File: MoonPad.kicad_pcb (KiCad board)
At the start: 4 copper layers, 44.4 x 40.6 mm, 61 parts, among them IC1 W25Q16JVUXIQ, J1 OLED, J3 USB-C 2.0 Receptacle, SW1 Reset, U3 RP2040, U4 Hall_Sensor, U5 Hall_Sensor, U6 AP2112K-3.3, Y1 JGHC S3212000181080

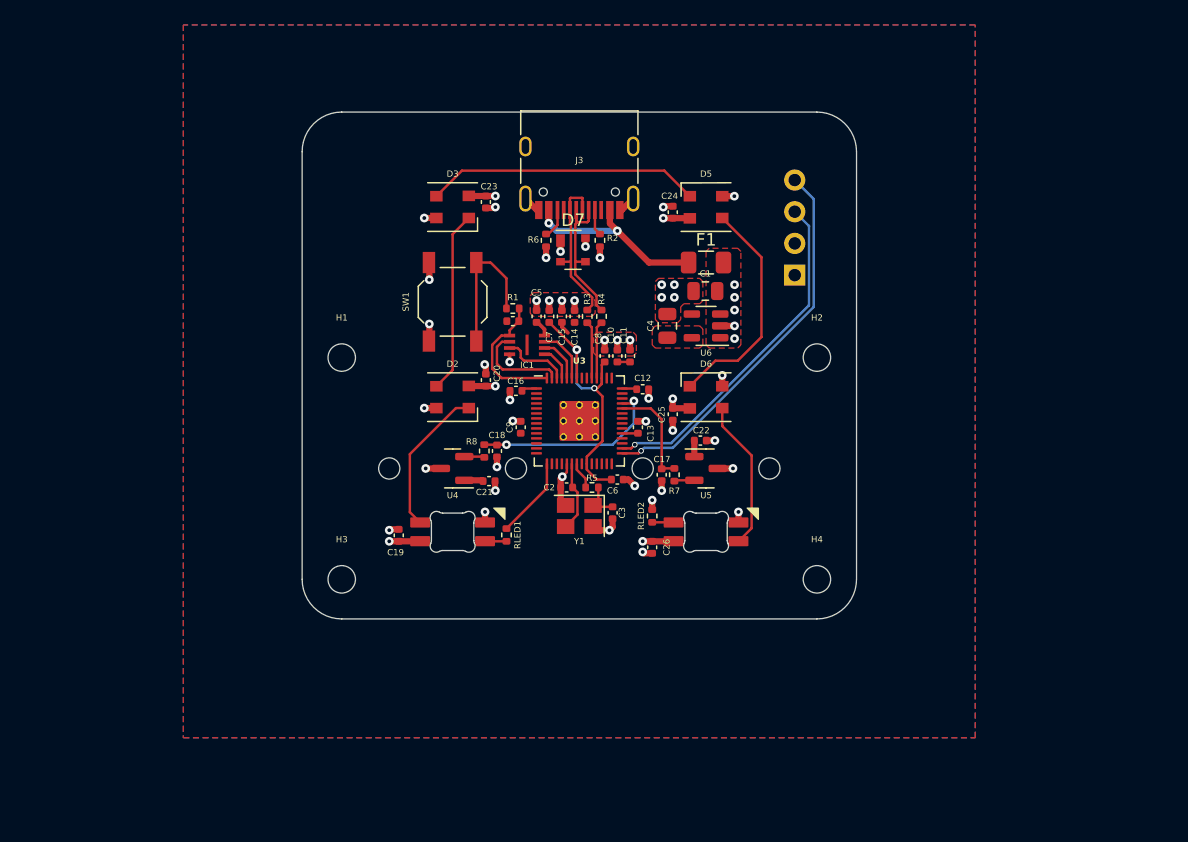
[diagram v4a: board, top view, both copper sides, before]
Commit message: Added part numbers, some schema adjustments
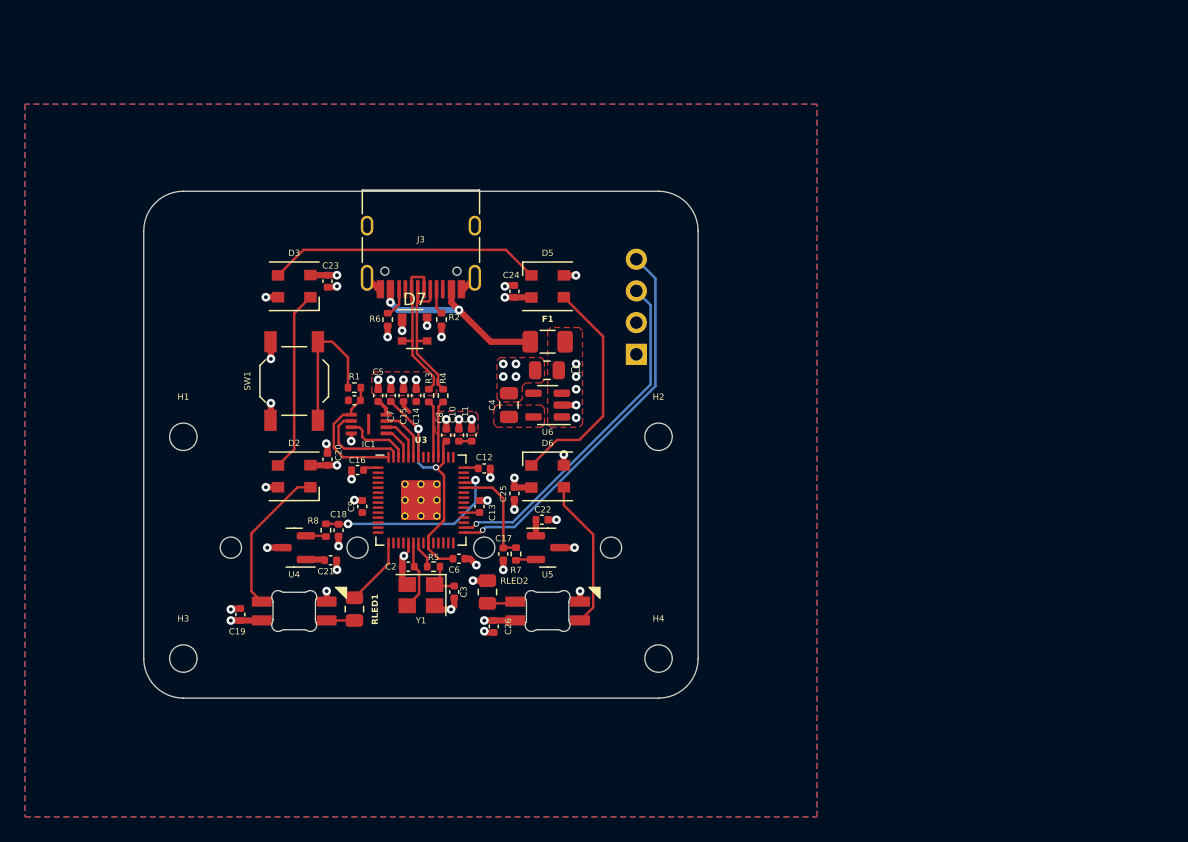
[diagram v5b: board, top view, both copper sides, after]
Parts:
- RLED1, RLED2: footprint Resistor_SMD:R_0402_1005Metric -> Resistor_SMD:R_0805_2012Metric
- moved RLED2 14.5 mm to (151.4, 109.0)
- moved C12 14.2 mm to (151.1, 99.1)
- moved C13 14.2 mm to (150.7, 102.1)
- moved C15 14.2 mm to (144.7, 93.2)
- moved C17 14.2 mm to (152.7, 105.9)
- moved C23 14.2 mm to (138.6, 84.0)
- moved C1 14.2 mm to (156.2, 91.2)
- moved C2 14.2 mm to (145.0, 106.9)
- moved C20 14.2 mm to (138.6, 98.3)
- moved C26 14.2 mm to (151.9, 111.7)
- moved C8 14.2 mm to (148.1, 96.4)
- moved D1 14.2 mm to (135.9, 105.4)
- moved D2 14.2 mm to (135.9, 99.7)
- moved D3 14.2 mm to (135.9, 84.5)
- moved H2 14.2 mm to (165.1, 96.5)
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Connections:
- net /GPIO12 renamed /RGB
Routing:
- net /RGB: track 6.54 -> 5.52 mm
- net Net-(D4-DOUT): track 1.72 -> 2.28 mm
- net Net-(D1-DIN): track 1.72 -> 2.23 mm
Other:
- board size 44.4 x 40.6 mm -> 44.5 x 40.6 mm

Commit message: Minor layout changes
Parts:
- moved C26 0.68 mm to (151.4, 111.3), turned to 180 degrees
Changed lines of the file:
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@@
     (property "ki_keywords" "cap capacitor")
     (attr smd)
-    (fp_text reference "C9" (at 0 -0.889 90) (layer "F.SilkS")
+    (fp_text reference "C9" (at 1.27 0 180) (layer "F.SilkS")
         (effects (font (size 0.5 0.5) (thickness 0.125)))
     )
@@
   )
   (footprint "Capacitor_SMD:C_0402_1005Metric" (layer "F.Cu")
-    (at 151.892 111.732 -90)
+    (at 151.412 111.252 180)
     (descr "Capacitor SMD 0402 (1005 Metric), square (rectangular) end terminal, IPC_7351 nominal, (Body size source: IPC-SM-782 page 76, https://www.pcb-3d.com/wordpress/wp-content/uploads/ipc-sm-782a_amendment_1_and_2.pdf), generated with kicad-footprint-generator")
     (tags "capacitor")
@@
     (property "ki_keywords" "cap capacitor")
     (attr smd)
-    (fp_text reference "C26" (at 0 -1.16 90) (layer "F.SilkS")
+    (fp_text reference "C26" (at 1.679 0) (layer "F.SilkS")
         (effects (font (size 0.5 0.5) (thickness 0.125)))
     )
-    (fp_text value "100n" (at 0 1.16 90) (layer "F.Fab")
+    (fp_text value "100n" (at 0 1.16) (layer "F.Fab")
         (effects (font (size 1 1) (thickness 0.15)))
     )
-    (fp_text user "${REFERENCE}" (at 0 0 90) (layer "F.Fab")
+    (fp_text user "${REFERENCE}" (at 0 0) (layer "F.Fab")
         (effects (font (size 0.25 0.25) (thickness 0.04)))
     )
@@
     (fp_line (start 0.5 0.25) (end -0.5 0.25)
       (stroke (width 0.1) (type solid)) (layer "F.Fab"))
-    (pad "1" smd roundrect (at -0.48 0 270) (size 0.56 0.62) (layers "F.Cu" "F.Paste" "F.Mask") (roundrect_rratio 0.25)
+    (pad "1" smd roundrect (at -0.48 0 180) (size 0.56 0.62) (layers "F.Cu" "F.Paste" "F.Mask") (roundrect_rratio 0.25)
       (net 1 "VBUS") (pintype "passive"))
-    (pad "2" smd roundrect (at 0.48 0 270) (size 0.56 0.62) (layers "F.Cu" "F.Paste" "F.Mask") (roundrect_rratio 0.25)
+    (pad "2" smd roundrect (at 0.48 0 180) (size 0.56 0.62) (layers "F.Cu" "F.Paste" "F.Mask") (roundrect_rratio 0.25)
       (net 2 "GND") (pintype "passive"))
     (model "${KICAD6_3DMODEL_DIR}/Capacitor_SMD.3dshapes/C_0402_1005Metric.wrl"
@@
     (property "ki_keywords" "cap capacitor")
     (attr smd)
-    (fp_text reference "C20" (at 0.536 0.889 270) (layer "F.SilkS")
+    (fp_text reference "C20" (at 0.536 0.889 90) (layer "F.SilkS")
         (effects (font (size 0.5 0.5) (thickness 0.125)))
     )
@@
     (property "ki_keywords" "cap capacitor")
     (attr smd)
-    (fp_text reference "C3" (at 0 -0.762 90) (layer "F.SilkS")
+    (fp_text reference "C3" (at 0 -1.016 -180) (layer "F.SilkS")
         (effects (font (size 0.5 0.5) (thickness 0.125)))
     )
@@
     (property "Sheetname" "")
     (attr smd)
-    (fp_text reference "U3" (at 0 -4.82) (layer "F.SilkS")
+    (fp_text reference "U3" (at 0 -4.572) (layer "F.SilkS")
         (effects (font (size 0.5 0.5) (thickness 0.125) bold))
     )
@@
     (property "ki_keywords" "R res resistor")
     (attr smd)
-    (fp_text reference "R5" (at 0 -0.762) (layer "F.SilkS")
+    (fp_text reference "R5" (at 0 -0.889) (layer "F.SilkS")
         (effects (font (size 0.5 0.5) (thickness 0.125)))
     )
@@
     (fp_arc (start -1.699999 -4.377158) (mid -1.712527 -4.265932) (end -1.749484 -4.16028)
       (stroke (width 0.1) (type solid)) (layer "Edge.Cuts"))
-    (fp_arc (start -1.046711 -3.511701) (mid -1.638072 -3.575966) (end -1.749484 -4.160281)
+    (fp_arc (start -1.046711 -3.511701) (mid -1.638071 -3.575966) (end -1.749484 -4.160281)
       (stroke (width 0.1) (type solid)) (layer "Edge.Cuts"))
     (fp_arc (start -1.046711 -3.511701) (mid -0.925123 -3.562624) (end -0.794452 -3.58)
@@
     (fp_arc (start 1.046711 -6.648299) (mid 1.638071 -6.584036) (end 1.749484 -5.99972)
       (stroke (width 0.1) (type solid)) (layer "Edge.Cuts"))
-    (fp_arc (start 1.699999 -5.782842) (mid 1.712528 -5.894068) (end 1.749484 -5.99972)
+    (fp_arc (start 1.699999 -5.782842) (mid 1.712527 -5.894068) (end 1.749484 -5.99972)
       (stroke (width 0.1) (type solid)) (layer "Edge.Cuts"))
     (fp_arc (start 1.749484 -4.16028) (mid 1.63807 -3.575966) (end 1.046711 -3.511703)
@@
     (fp_arc (start -1.699999 -4.377158) (mid -1.712527 -4.265932) (end -1.749484 -4.16028)
       (stroke (width 0.1) (type solid)) (layer "Edge.Cuts"))
-    (fp_arc (start -1.046711 -3.511701) (mid -1.638072 -3.575966) (end -1.749484 -4.160281)
+    (fp_arc (start -1.046711 -3.511701) (mid -1.638071 -3.575966) (end -1.749484 -4.160281)
       (stroke (width 0.1) (type solid)) (layer "Edge.Cuts"))
     (fp_arc (start -1.046711 -3.511701) (mid -0.925123 -3.562624) (end -0.794452 -3.58)
@@
     (fp_arc (start 1.046711 -6.648299) (mid 1.638071 -6.584036) (end 1.749484 -5.99972)
       (stroke (width 0.1) (type solid)) (layer "Edge.Cuts"))
-    (fp_arc (start 1.699999 -5.782842) (mid 1.712528 -5.894068) (end 1.749484 -5.99972)
+    (fp_arc (start 1.699999 -5.782842) (mid 1.712527 -5.894068) (end 1.749484 -5.99972)
       (stroke (width 0.1) (type solid)) (layer "Edge.Cuts"))
     (fp_arc (start 1.749484 -4.16028) (mid 1.63807 -3.575966) (end 1.046711 -3.511703)
@@
       (rotate (xyz 0 0 0))
     )
+    (model "${KIPRJMOD}/Libraries/kicad-keyboard-parts.pretty/3d/LED_SK6812MINI-E.step"
+      (offset (xyz 0 0 0))
+      (scale (xyz 1 1 1))
+      (rotate (xyz 0 0 0))
+    )
   )
   (footprint "Button_Switch_Keyboard:Wooting_1.00u" (layer "B.Cu")
@@
   (segment (start 131.572 111.252) (end 133.278 111.252) (width 0.5) (layer "F.Cu") (net 1))
   (segment (start 153.543 100.584) (end 154.899 100.584) (width 0.5) (layer "F.Cu") (net 1))
-  (segment (start 151.892 111.252) (end 151.13 111.252) (width 0.5) (layer "F.Cu") (net 1))
+  (segment (start 151.892 111.252) (end 151.892 112.014) (width 0.5) (layer "F.Cu") (net 1))
   (segment (start 138.557 98.806) (end 139.319 98.806) (width 0.5) (layer "F.Cu") (net 1))
   (segment (start 138.557 83.566) (end 137.201 83.566) (width 0.5) (layer "F.Cu") (net 1))
@@
   (via (at 139.319 83.566) (size 0.7) (drill 0.3) (layers "F.Cu" "B.Cu") (net 1))
   (via (at 158.496 91.694) (size 0.7) (drill 0.3) (layers "F.Cu" "B.Cu") (free) (net 1))
-  (via (at 151.13 111.252) (size 0.7) (drill 0.3) (layers "F.Cu" "B.Cu") (net 1))
+  (via (at 151.892 112.014) (size 0.7) (drill 0.3) (layers "F.Cu" "B.Cu") (net 1))
   (via (at 146.542 87.614) (size 0.7) (drill 0.3) (layers "F.Cu" "B.Cu") (net 1))
   (via (at 158.496 94.995996) (size 0.7) (drill 0.3) (layers "F.Cu" "B.Cu") (free) (net 1))
@@
   (via (at 130.81 111.252) (size 0.7) (drill 0.3) (layers "F.Cu" "B.Cu") (net 1))
   (via (at 158.496001 90.678) (size 0.7) (drill 0.3) (layers "F.Cu" "B.Cu") (free) (net 1))
+  (segment (start 150.932 111.905903) (end 150.932 111.252) (width 0.5) (layer "F.Cu") (net 2))
   (segment (start 144.554 107.974) (end 144.554 106.934) (width 0.5) (layer "F.Cu") (net 2))
   (segment (start 139.446 104.493) (end 139.446 105.283) (width 0.5) (layer "F.Cu") (net 2))
@@
   (segment (start 139.291 107.16) (end 139.319 107.188) (width 0.5) (layer "F.Cu") (net 2))
   (segment (start 152.852 84.384) (end 152.781 84.455) (width 0.5) (layer "F.Cu") (net 2))
+  (segment (start 151.040097 112.014) (end 150.932 111.905903) (width 0.5) (layer "F.Cu") (net 2))
   (segment (start 148.082 95.913) (end 148.082 95.123) (width 0.5) (layer "F.Cu") (net 2))
   (segment (start 133.618 85.33) (end 134.59 85.33) (width 0.5) (layer "F.Cu") (net 2))
@@
   (segment (start 150.2175 108.0535) (end 151.384 108.0535) (width 0.5) (layer "F.Cu") (net 2))
   (segment (start 144.687289 106.070887) (end 144.554 106.204176) (width 0.5) (layer "F.Cu") (net 2))
-  (segment (start 151.238097 112.212) (end 151.892 112.212) (width 0.5) (layer "F.Cu") (net 2))
   (segment (start 151.61 99.794) (end 151.61 99.06) (width 0.5) (layer "F.Cu") (net 2))
   (segment (start 149.455 84.69) (end 150.37 83.775) (width 0.5) (layer "F.Cu") (net 2))
@@
   (segment (start 134.026102 88.900001) (end 134.026103 90.267) (width 0.5) (layer "F.Cu") (net 2))
   (segment (start 158.81 108.894135) (end 158.81 109.74) (width 0.5) (layer "F.Cu") (net 2))
-  (segment (start 151.13 112.103903) (end 151.238097 112.212) (width 0.5) (layer "F.Cu") (net 2))
   (segment (start 149.987 106.299) (end 150.495 106.807) (width 0.5) (layer "F.Cu") (net 2))
   (segment (start 147.443 110.363) (end 147.15 110.07) (width 0.5) (layer "F.Cu") (net 2))
@@
   (via (at 148.082 95.123) (size 0.7) (drill 0.3) (layers "F.Cu" "B.Cu") (net 2))
   (via (at 152.781 84.455) (size 0.7) (drill 0.3) (layers "F.Cu" "B.Cu") (net 2))
-  (via (at 151.13 112.103903) (size 0.7) (drill 0.3) (layers "F.Cu" "B.Cu") (net 2))
+  (via (at 151.040097 112.014) (size 0.7) (drill 0.3) (layers "F.Cu" "B.Cu") (net 2))
   (via (at 143.637 91.948) (size 0.7) (drill 0.3) (layers "F.Cu" "B.Cu") (net 2))
   (via (at 158.369 105.41) (size 0.7) (drill 0.3) (layers "F.Cu" "B.Cu") (net 2))

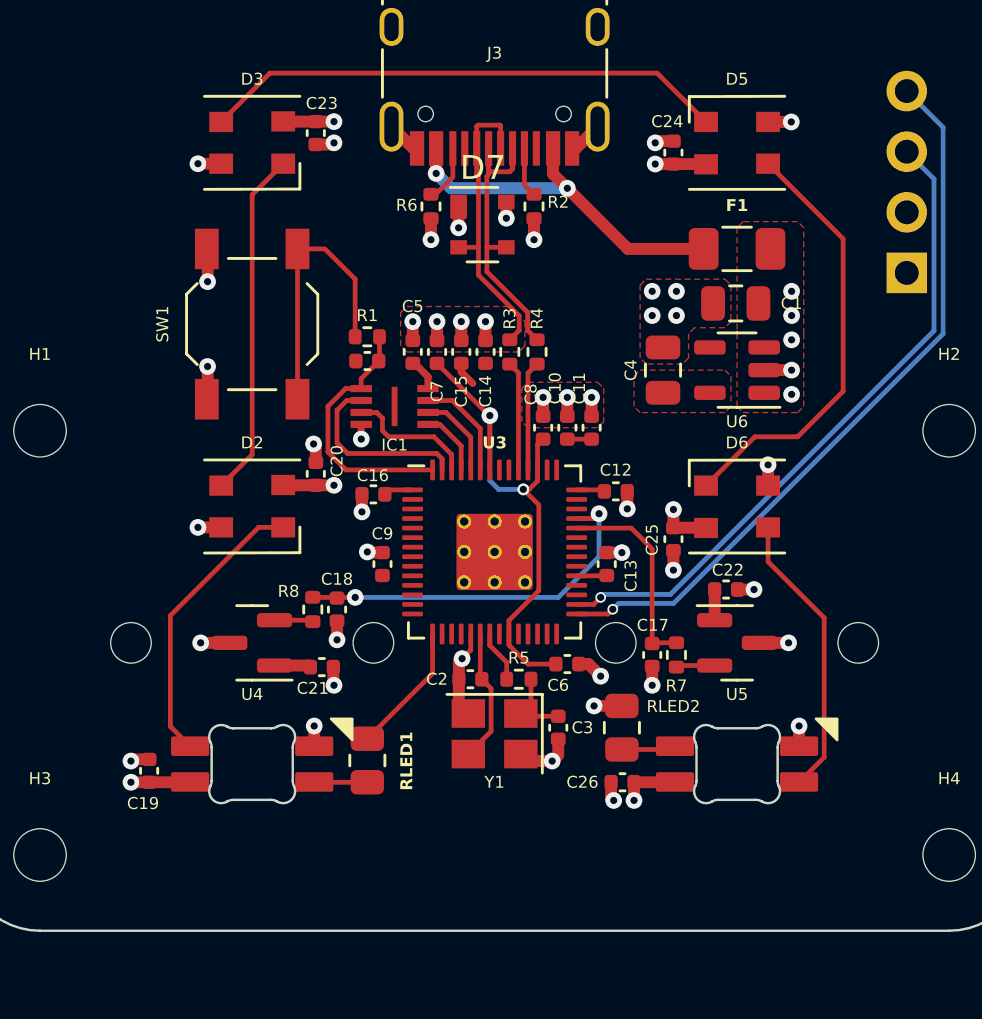
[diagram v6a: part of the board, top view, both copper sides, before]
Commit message: All part numbers added
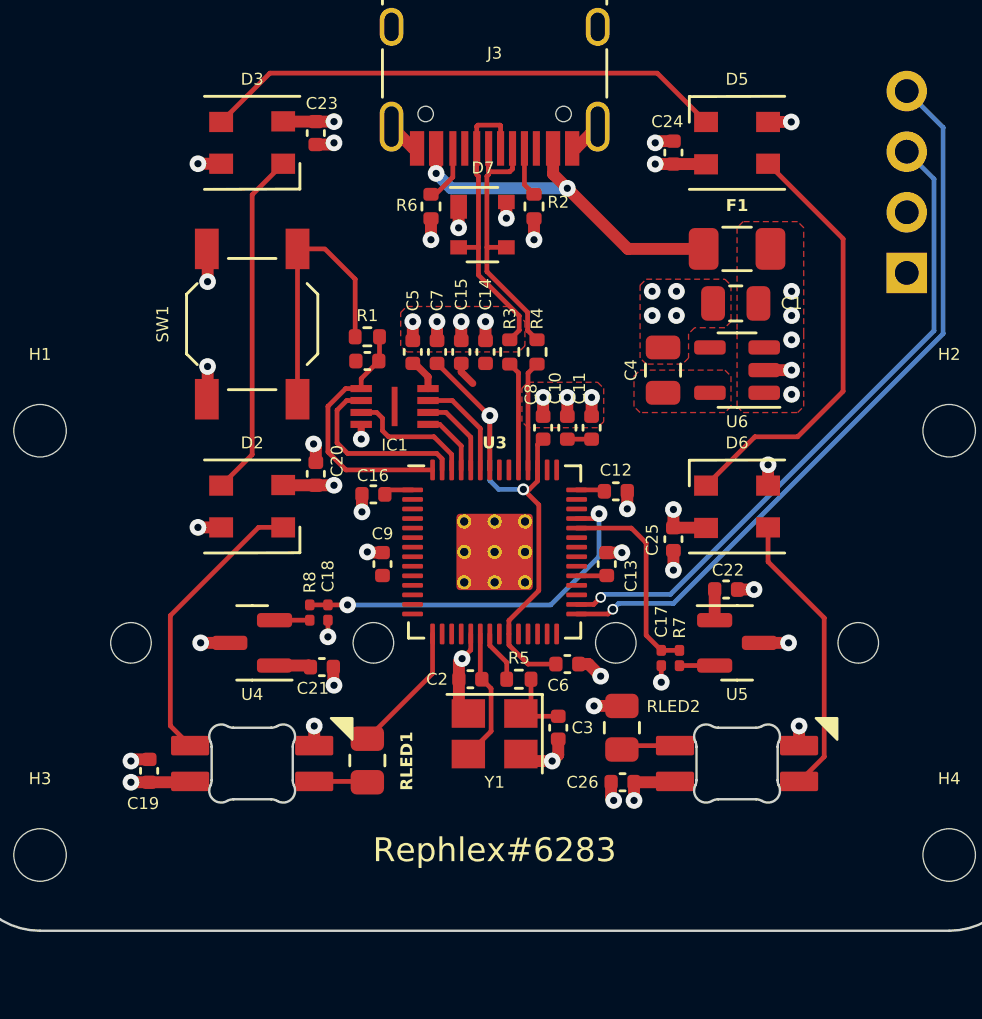
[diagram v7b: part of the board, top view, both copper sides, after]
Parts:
- C17, C18: footprint Capacitor_SMD:C_0402_1005Metric -> Capacitor_SMD:C_0201_0603Metric
- D1, D4: moved to F.Cu
- F1: value Polyfuse -> 1.1A
- R7, R8: footprint Resistor_SMD:R_0402_1005Metric -> Resistor_SMD:R_0201_0603Metric
- U4, U5: value Hall_Sensor -> SLSS49E-3
- moved D1 5.08 mm to (135.9, 110.5), turned to 0 degrees
- moved D4 5.08 mm to (156.2, 110.5), turned to 0 degrees
- moved C17 0.40 mm to (153.0, 106.0)
- moved C18 0.40 mm to (139.1, 104.1)
- moved R7 0.18 mm to (153.8, 106.0)
- moved R8 0.18 mm to (138.3, 104.1)
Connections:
- C1 pad 1: VBUS -> +5V
- C19 pad 1: VBUS -> +5V
- C20 pad 1: VBUS -> +5V
- C23 pad 1: VBUS -> +5V
- C24 pad 1: VBUS -> +5V
- C25 pad 1: VBUS -> +5V
- C26 pad 1: VBUS -> +5V
- D1 pad 1: VBUS -> +5V
- D2 pad 2: VBUS -> +5V
- D3 pad 2: VBUS -> +5V
- D4 pad 1: VBUS -> +5V
- D5 pad 2: VBUS -> +5V
- D6 pad 2: VBUS -> +5V
- D7 pad 4: VBUS -> +5V
- F1 pad 1: /Fuse -> VBUS
- F1 pad 2: VBUS -> +5V
- J3 pad A4: /Fuse -> VBUS
- J3 pad A9: /Fuse -> VBUS
- J3 pad B4: /Fuse -> VBUS
- J3 pad B9: /Fuse -> VBUS
- U6 pad 1: VBUS -> +5V
- U6 pad 3: VBUS -> +5V
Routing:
- net /Fuse: track 15.5 -> 0.00 mm, vias 2 -> 0
- net +5V: track 0.00 -> 14.2 mm, vias 0 -> 11
- net VBUS: track 14.2 -> 15.5 mm, vias 11 -> 2
- added copper zone on B.Cu, net +5V
- added copper zone on F.Cu, net +5V
- removed copper zone on B.Cu, net VBUS
- removed copper zone on F.Cu, net VBUS
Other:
- board text added: "Rephlex#6283"

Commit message: Less extended parts
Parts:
- removed OLED: OLED, Moonpad:OLED 0.91
- added C27: 100n, Capacitor_SMD:C_0402_1005Metric, F.Cu at (149.1, 107.3)
- C17, C18: value 0.1u -> 100n; footprint Capacitor_SMD:C_0201_0603Metric -> Capacitor_SMD:C_0402_1005Metric
- R7, R8: footprint Resistor_SMD:R_0201_0603Metric -> Resistor_SMD:R_0402_1005Metric
- RLED1, RLED2: value 500 -> 470; footprint Resistor_SMD:R_0805_2012Metric -> Resistor_SMD:R_0402_1005Metric
- moved C3 1.27 mm to (148.7, 110.2)
- moved C2 1.27 mm to (145.0, 108.2)
- moved R5 1.27 mm to (147.1, 108.2)
- moved Y1 1.27 mm to (146.1, 110.5)
- moved C8 0.74 mm to (148.6, 95.9)
- moved C10 0.74 mm to (149.7, 95.9)
- moved C11 0.74 mm to (150.7, 95.9)
- moved RLED1 0.65 mm to (140.2, 110.7)
- moved RLED2 0.57 mm to (151.9, 109.2)
- moved C17 0.46 mm to (152.7, 105.8)
- moved C18 0.40 mm to (139.4, 104.0)
- moved R7 0.29 mm to (153.7, 105.8)
- moved R8 0.18 mm to (138.4, 104.0)
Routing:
- net +3V3: track 10.0 -> 20.2 mm
- net GND: track 42.3 -> 44.1 mm, vias 44 -> 46
- net +1V1: track 21.9 -> 23.2 mm
- net /XIN: track 5.61 -> 6.88 mm
- net /XOUT: track 2.19 -> 3.46 mm
- net Net-(D5-DOUT): track 18.2 -> 19.4 mm
- net /RGB: track 5.52 -> 6.54 mm
- net ADC_X: track 15.8 -> 14.8 mm
- net ADC_Z: track 8.70 -> 8.06 mm
- net Net-(D4-DOUT): track 2.27 -> 1.70 mm
- net /OLED_SCL: track 27.7 -> 28.2 mm
- net /OLED_SDA: track 31.0 -> 31.5 mm
- net Net-(D1-DIN): track 2.24 -> 1.73 mm
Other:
- board text added: "Rephlex"
- board text removed: "Rephlex#6283"
